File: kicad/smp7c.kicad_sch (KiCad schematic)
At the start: 16 parts, among them J1 Conn_01x06, J2 Micro_SD_Card_Det, J3 Conn_01x08, Q1 Q_NMOS_GSD (IRLML2502), Q2 Q_PMOS_GSD (AO3401), U1 ESP32-WROOM-32, U2 XC6206p332MR

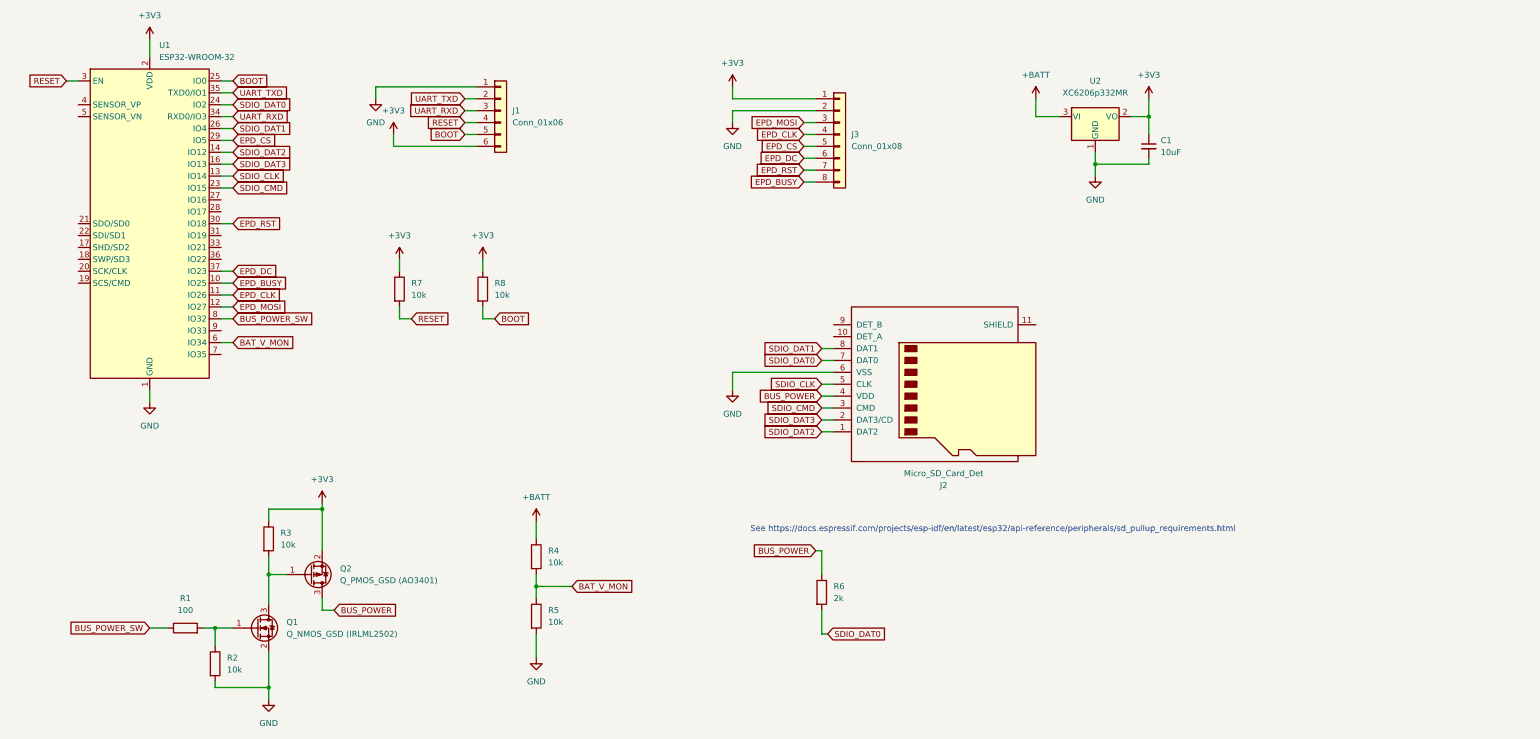
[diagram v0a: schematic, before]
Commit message: Implement battery voltage monitoring feature
- Update schematic to have voltage divider for monitoring
- Update firmware to monitor voltage and show low voltage notification
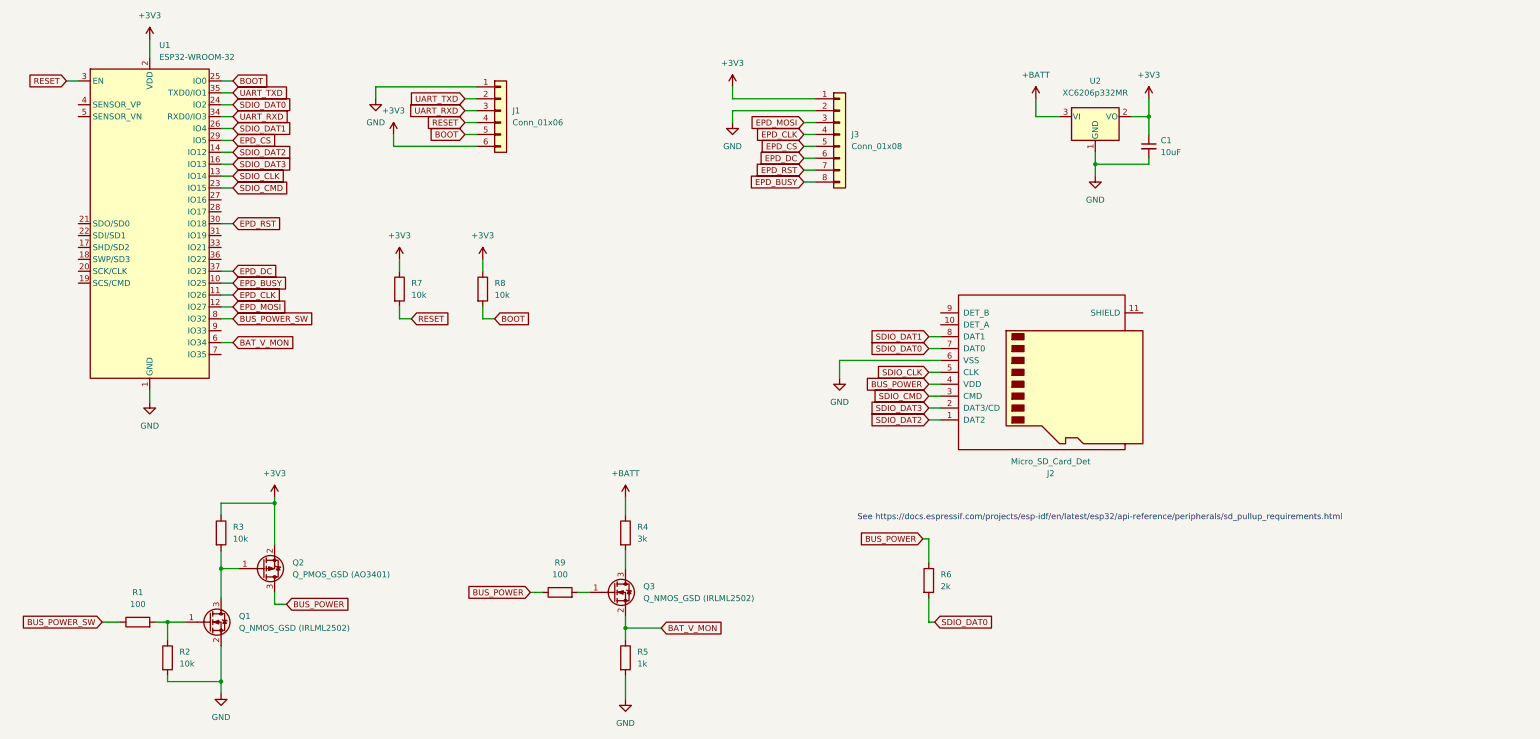
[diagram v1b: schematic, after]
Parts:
- added Q3: Q_NMOS_GSD (IRLML2502), Package_TO_SOT_SMD:SOT-23, symbol Device:Q_NMOS_GSD
- added R9: 100, Resistor_SMD:R_0603_1608Metric, symbol Device:R
- R4: value 10k -> 3k
- R5: value 10k -> 1k
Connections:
- net BAT_V_MON: now also Q3.2 (S); no longer R4.2
- net BUS_POWER: now also R9.1
- new net: Q3.1 (G), R9.2
- new net: Q3.3 (D), R4.2
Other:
- moved on the sheet: J2, Q1, Q2, R1, R2, R3, R4, R6
